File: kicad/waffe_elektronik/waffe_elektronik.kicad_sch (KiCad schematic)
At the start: 61 parts, among them J1 WS2812 HP-Streifen, J2 GX16-7pol, M1 Vibromotor Rueckstoß, M2 Vibromotor Treffer, Q1 AO3400A, Q2 AO3400A, Q3 AO3400A, SW1 Taster, SW2 Taster, U1 Boost_5V_MT3608, U10 TSOP34838, U11 TSOP34838, U2 AMS1117-3.3, U3 MCP73831, U4 ESP32S3_DevKitC, U5 74AHCT125, U6 MAX98357A, U7 TSOP34838, U8 TSOP34838, U9 TSOP34838

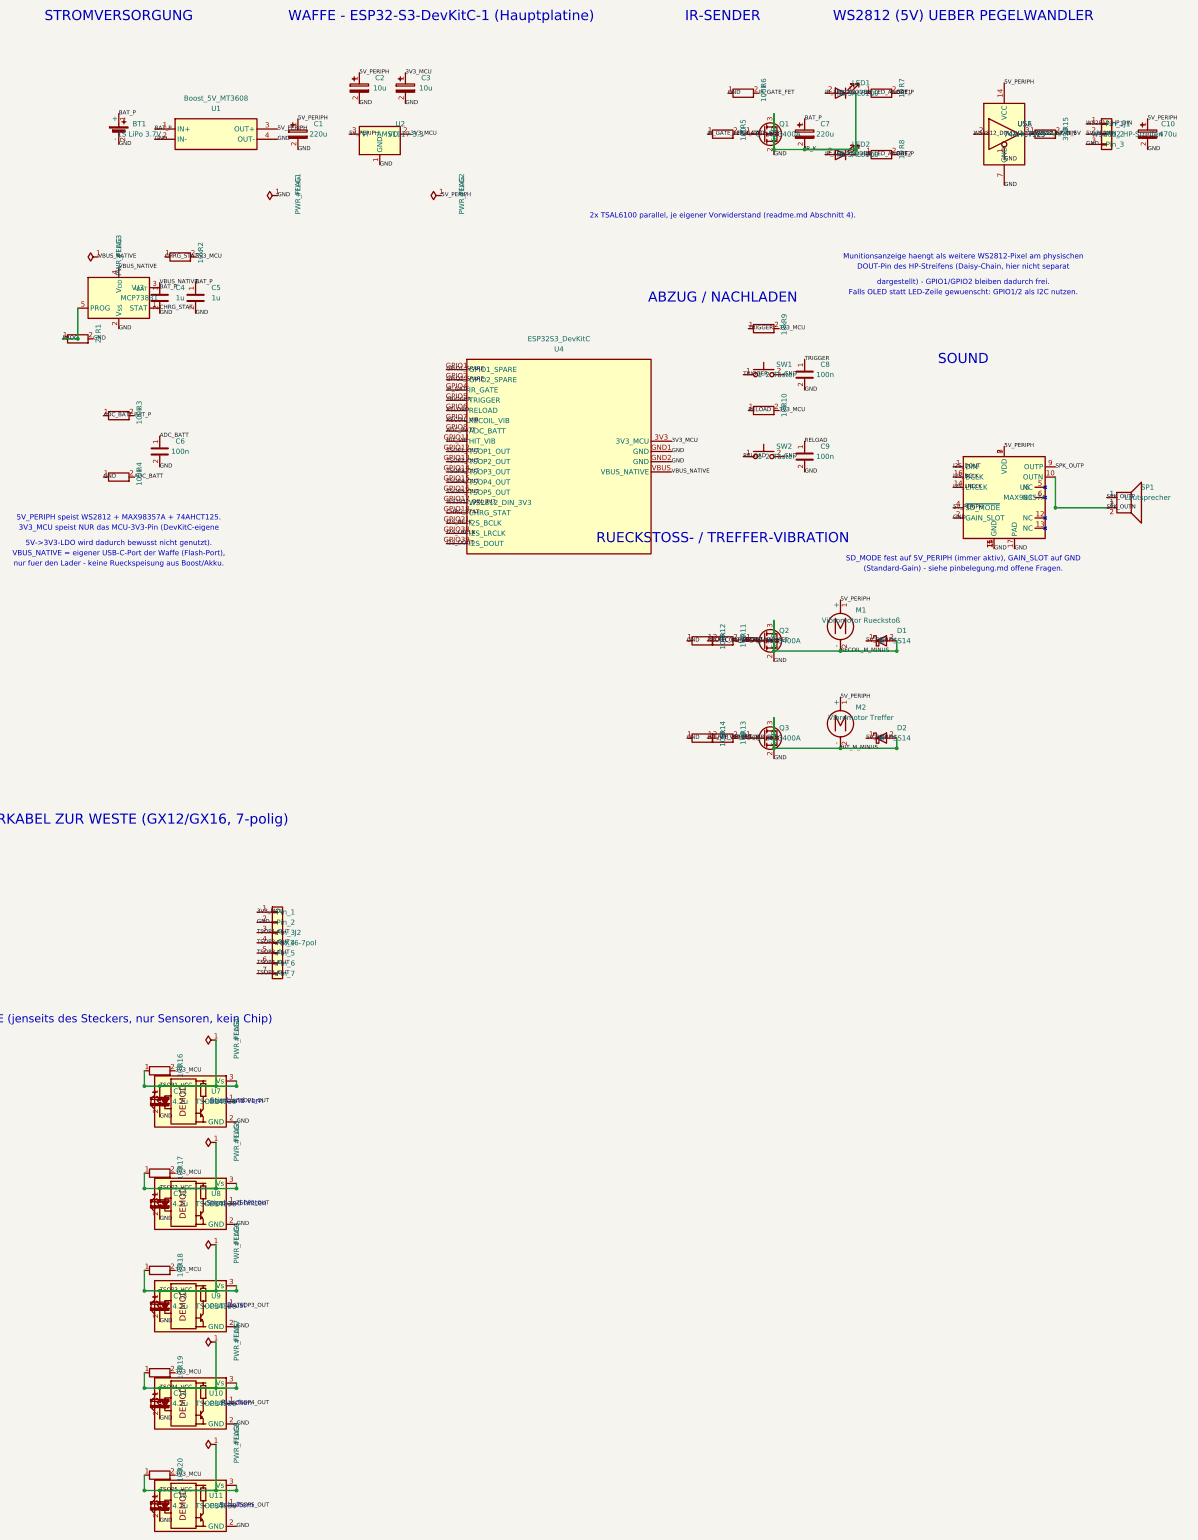
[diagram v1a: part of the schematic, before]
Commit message: Verdrahte alle Signalnetze echt (inkl. MCU-Läufe) statt nur lokaler Cluster
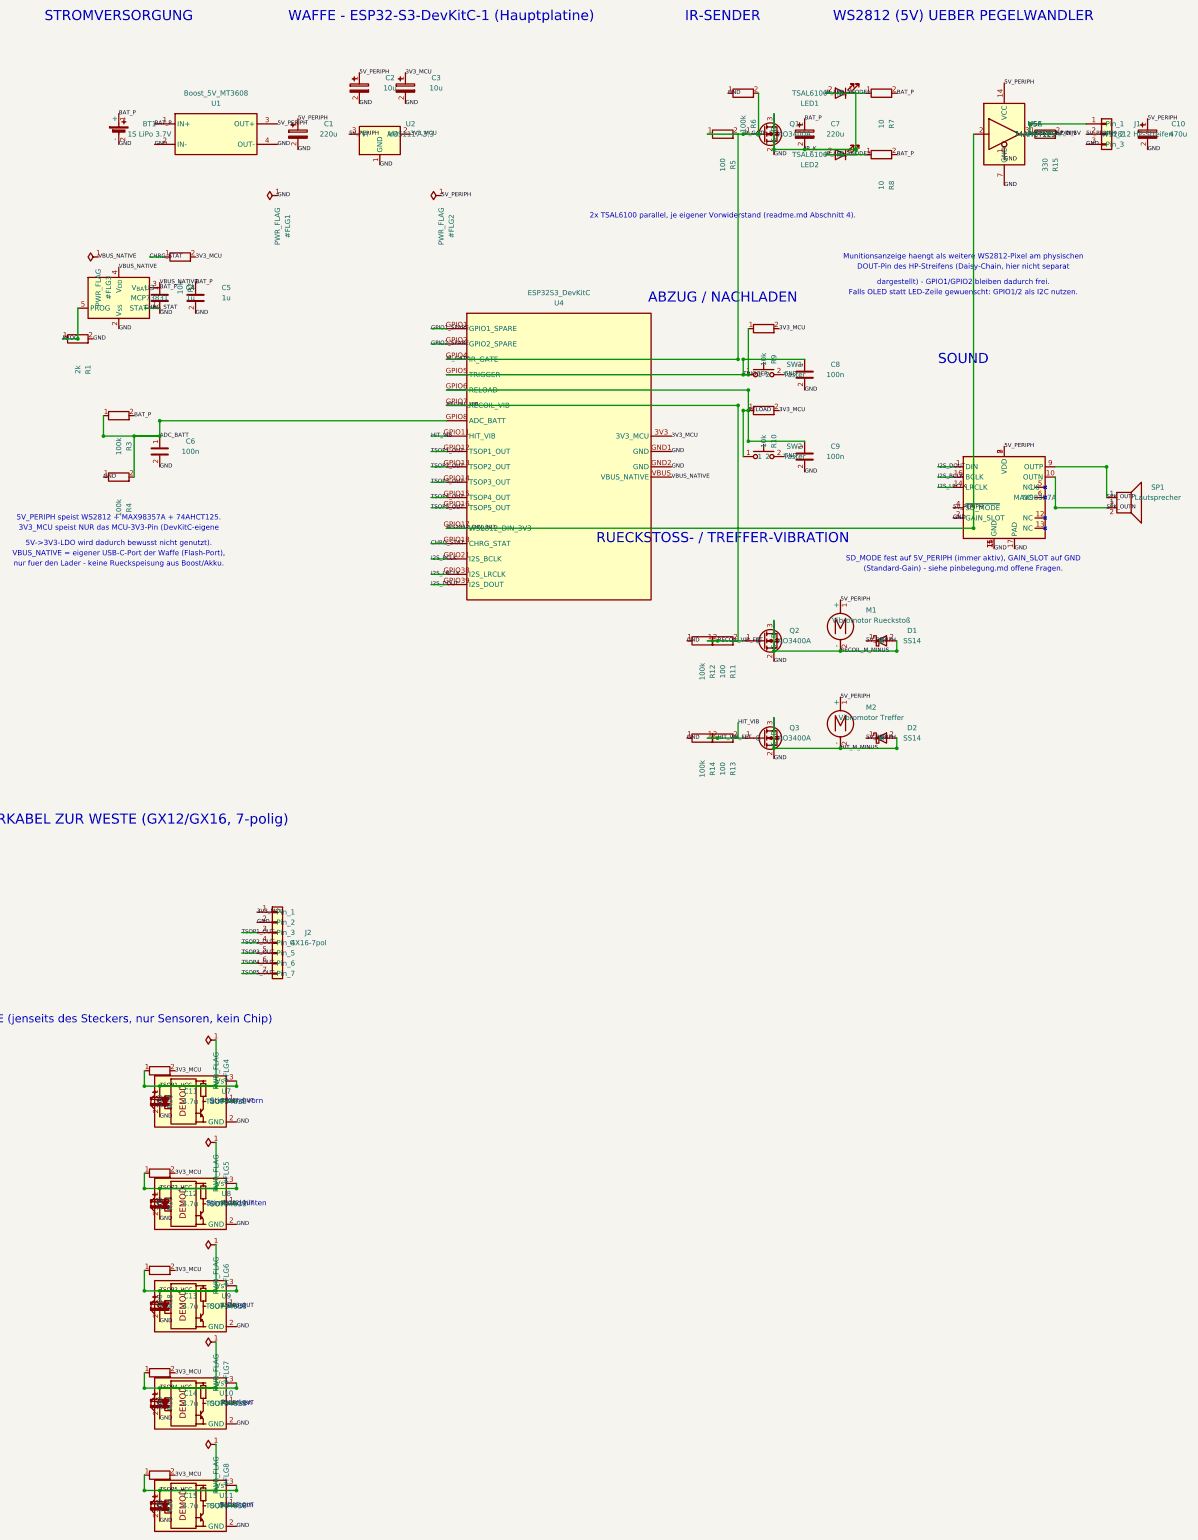
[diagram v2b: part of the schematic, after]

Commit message: Zeichne Schaltplan neu: Funktionsblöcke, saubere Verdrahtung, A3
Blöcke gerahmt, Versorgung oben/Masse unten, Signale zwischen Blöcken über
Labels an kurzen Stichleitungen. Unbenutzte 74AHCT125-Gatter auf GND,
GPIO1/2 als No-Connect. Vorschaubild in der README.
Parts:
- added unit 3 of U5
- added unit 2 of U5
- added unit 4 of U5
- BT1: value 1S LiPo 3.7V -> 1S LiPo 3,7 V
- J2: value GX16-7pol -> GX16 7-polig
- M1: value Vibromotor Rueckstoß -> Vibromotor Rückstoss
- U1: value Boost_5V_MT3608 -> MT3608 Boost 5 V
- U4: value ESP32S3_DevKitC -> ESP32-S3-DevKitC-1
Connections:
- net 3V3_MCU: now also R10.1, R16.1, R17.1, R18.1, R19.1, R2.1, R20.1, R9.1; no longer R10.2, R16.2, R17.2, R18.2, R19.2, R2.2, R20.2, R9.2
- net ADC_BATT: now also R3.2, R4.1; no longer R3.1, R4.2
- net BAT_P: now also R3.1, R7.1, R8.1; no longer R3.2, R7.2, R8.2
- net CHRG_STAT: now also R2.2; no longer R2.1
- net GND: now also R12.2, R14.2, R4.2, R6.2, U5.10, U5.12, U5.13, U5.4, U5.5, U5.9; no longer R12.1, R14.1, R4.1, R6.1
- net HIT_VIB: now also R13.1; no longer R13.2
- net IR_GATE: now also R5.1; no longer R5.2
- net RECOIL_VIB: now also R11.1; no longer R11.2
- net RELOAD: now also R10.2; no longer R10.1
- net TRIGGER: now also R9.2; no longer R9.1
- net GPIO1_SPARE: no longer names the net of U4.GPIO1
- net GPIO2_SPARE: no longer names the net of U4.GPIO2
- net HIT_M_MINUS: no longer names the net of D2.2 (A), M2.2 (-), Q3.3 (D)
- removed net HIT_VIB_FET: Q3.1 (G), R13.1, R14.2
- removed net IR_GATE_FET: Q1.1 (G), R5.1, R6.2
- net IR_K: no longer names the net of C7.2, LED1.1 (K), LED2.1 (K), Q1.3 (D)
- net IR_LED_ANODE1: no longer names the net of LED1.2 (A)
- net IR_LED_ANODE1: now also R7.2; no longer R7.1
- net IR_LED_ANODE2: no longer names the net of LED2.2 (A)
- net IR_LED_ANODE2: now also R8.2; no longer R8.1
- net PROG: no longer names the net of R1.1, U3.5 (PROG)
- net RECOIL_M_MINUS: no longer names the net of D1.2 (A), M1.2 (-), Q2.3 (D)
- removed net RECOIL_VIB_FET: Q2.1 (G), R11.1, R12.2
- net SPK_OUTN: no longer names the net of SP1.2, U6.10 (OUTN)
- net SPK_OUTP: no longer names the net of SP1.1, U6.9 (OUTP)
- net TSOP1_VCC: no longer names the net of C11.1, U7.3 (Vs)
- net TSOP1_VCC: now also R16.2; no longer R16.1
- net TSOP2_VCC: no longer names the net of C12.1, U8.3 (Vs)
- net TSOP2_VCC: now also R17.2; no longer R17.1
- net TSOP3_VCC: no longer names the net of C13.1, U9.3 (Vs)
- net TSOP3_VCC: now also R18.2; no longer R18.1
- net TSOP4_VCC: no longer names the net of C14.1, U10.3 (Vs)
- net TSOP4_VCC: now also R19.2; no longer R19.1
- net TSOP5_VCC: no longer names the net of C15.1, U11.3 (Vs)
- net TSOP5_VCC: now also R20.2; no longer R20.1
- net WS2812_DIN_5V: no longer names the net of U5.3
- net WS2812_DIN_5V: now also R15.1; no longer R15.2
- net WS2812_HP_DIN: no longer names the net of J1.1 (Pin_1)
- net WS2812_HP_DIN: now also R15.2; no longer R15.1
- new net: Q1.1 (G), R5.2, R6.1
- new net: Q3.1 (G), R13.2, R14.1
- new net: Q2.1 (G), R11.2, R12.1
- no-connect marks 0 -> 5
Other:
- note added: "Abzug / Nachladen"
- note added: "Akku-Messung"
- note added: "ESP32-S3 (Hauptplatine)"
- note added: "GPIO1/2 frei (Munitions-LED / I²C)"
- note added: "IR-Sender (2× TSAL6100 parallel)"
- note added: "Laden (USB-C Flash-Port)"
- note added: "Rücken"
- note added: "Rückstoss- / Treffer-Vibration"
- note added: "Sensorkabel zur Weste"
- note added: "Sound (I²S)"
- note added: "Stromversorgung"
- note added: "WS2812 (5 V) über Pegelwandler"
- note added: "Weste (nur Sensoren, jenseits des Steckers)"
- note added: "unbenutzte Gatter: Eingänge + /OE auf GND"
- note removed: "(Standard-Gain) - siehe pinbelegung.md offene Fragen."
- note removed: "2x TSAL6100 parallel, je eigener Vorwiderstand (readme.md Abschnitt 4)."
- note removed: "3V3_MCU speist NUR das MCU-3V3-Pin (DevKitC-eigene"
- note removed: "5V->3V3-LDO wird dadurch bewusst nicht genutzt)."
- note removed: "5V_PERIPH speist WS2812 + MAX98357A + 74AHCT125."
- note removed: "ABZUG / NACHLADEN"
- note removed: "DOUT-Pin des HP-Streifens (Daisy-Chain, hier nicht separat"
- note removed: "Falls OLED statt LED-Zeile gewuenscht: GPIO1/2 als I2C nutzen."
- note removed: "IR-SENDER"
- note removed: "Munitionsanzeige haengt als weitere WS2812-Pixel am physischen"
- note removed: "RUECKSTOSS- / TREFFER-VIBRATION"
- note removed: "Ruecken"
- note removed: "SD_MODE fest auf 5V_PERIPH (immer aktiv), GAIN_SLOT auf GND"
- note removed: "SENSORKABEL ZUR WESTE (GX12/GX16, 7-polig)"
- note removed: "SOUND"
- note removed: "STROMVERSORGUNG"
- note removed: "VBUS_NATIVE = eigener USB-C-Port der Waffe (Flash-Port),"
- note removed: "WAFFE - ESP32-S3-DevKitC-1 (Hauptplatine)"
- note removed: "WESTE (jenseits des Steckers, nur Sensoren, kein Chip)"
- note removed: "WS2812 (5V) UEBER PEGELWANDLER"
- note removed: "dargestellt) - GPIO1/GPIO2 bleiben dadurch frei."
- note removed: "nur fuer den Lader - keine Rueckspeisung aus Boost/Akku."
- company: (none) -> open-lasertag
- title: (none) -> Lasertag - Waffen-Elektronik

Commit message: ESP32-S3-WROOM-1 direkt auf der Platine, eigene USB-C-Buchse mit Auto-Flash
USB-C am nativen USB (IO19/IO20) mit CC-Widerständen und USBLC6-ESD-Schutz,
EN-RC-Glied, RESET- und BOOT-Taster. Flashen über USB-Serial-JTAG ohne
Wandlerchip. Doku und Stückliste angepasst.
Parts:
- removed U4: ESP32-S3-DevKitC-1, symbol Module:ESP32S3_DevKitC
- added C16: 1u, symbol Device:C
- added C17: 100n, symbol Device:C
- added C18: 10u, symbol Device:C
- added J3: USB-C (Flashen + Laden), symbol Connector:USB_C_Receptacle_USB2.0_16P
- added R21: 10k, symbol Device:R
- added R22, R23: 5.1k, symbol Device:R
- added SW3: RESET, symbol Switch:SW_Push
- added SW4: BOOT, symbol Switch:SW_Push
- added U12: USBLC6-2SC6, symbol Power_Protection:USBLC6-2SC6
- added U4: ESP32-S3-WROOM-1-N16R8, symbol RF_Module:ESP32-S3-WROOM-1
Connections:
- net 3V3_MCU: now also C17.1, C18.1, R21.1, U4.2 (3V3)
- net ADC_BATT: now also U4.12 (IO8)
- net CHRG_STAT: now also U4.11 (IO18)
- net GND: now also C16.2, C17.2, C18.2, J3.A1 (GND), J3.A12 (GND), J3.B1 (GND), J3.B12 (GND), J3.SH (SHIELD), R22.2, R23.2, SW3.1, SW4.1, U12.2 (GND), U4.1 (GND), U4.40 (GND), U4.41 (GND)
- net HIT_VIB: now also U4.19 (IO11)
- net I2S_BCLK: now also U4.23 (IO21)
- net I2S_DOUT: now also U4.32 (IO39)
- net I2S_LRCLK: now also U4.31 (IO38)
- net IR_GATE: now also U4.4 (IO4)
- net RECOIL_VIB: now also U4.7 (IO7)
- net RELOAD: now also U4.6 (IO6)
- net TRIGGER: now also U4.5 (IO5)
- net TSOP1_OUT: now also U4.20 (IO12)
- net TSOP2_OUT: now also U4.21 (IO13)
- net TSOP3_OUT: now also U4.22 (IO14)
- net TSOP4_OUT: now also U4.8 (IO15)
- net TSOP5_OUT: now also U4.9 (IO16)
- net VBUS_NATIVE: now also J3.A4 (VBUS), J3.A9 (VBUS), J3.B4 (VBUS), J3.B9 (VBUS), U12.5 (VBUS)
- net WS2812_DIN_3V3: now also U4.10 (IO17)
- new net: J3.A5 (CC1), R23.1
- new net: J3.A6 (D+), J3.B6 (D+), U12.3 (I/O2)
- new net: J3.A7 (D-), J3.B7 (D-), U12.1 (I/O1)
- new net: J3.B5 (CC2), R22.1
- new net: C16.1, R21.2, SW3.2, U4.3 (EN)
- new net: SW4.2, U4.27 (IO0)
- new net USB_D+: U12.4 (I/O2), U4.14 (USB_D+)
- new net USB_D-: U12.6 (I/O1), U4.13 (USB_D-)
- no-connect marks 5 -> 22
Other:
- note added: "ESP32-S3-WROOM-1"
- note added: "IO40 reserviert: TSOP 6 (Waffe vorne)"
- note added: "Laden (USB-C)"
- note added: "USB-C (nativer USB des ESP32-S3)"
- note added: "frei: IO1/IO2 (Munitions-LED / I²C), IO9/IO10, IO41/42, IO47/48"
- note removed: "ESP32-S3 (Hauptplatine)"
- note removed: "GPIO1/2 frei (Munitions-LED / I²C)"
- note removed: "Laden (USB-C Flash-Port)"

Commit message: Platine: 4 Lagen, nur SMD, von Hand geroutet; GPIOs layoutgetrieben neu zugeordnet
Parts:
- removed C1, C7: 220u, symbol Device:C_Polarized
- removed C10: 470u, symbol Device:C_Polarized
- removed C2: 10u, symbol Device:C_Polarized
- removed U1: MT3608 Boost 5 V, symbol Module:Boost_5V_MT3608
- added C1, C10, C7: 100u, Capacitor_SMD:C_1210_3225Metric, symbol Device:C
- added C19, C20: 22u, Capacitor_SMD:C_0805_2012Metric, symbol Device:C
- added C2, C22: 10u, Capacitor_SMD:C_0805_2012Metric, symbol Device:C
- added C21, C23: 100n, Capacitor_SMD:C_0603_1608Metric, symbol Device:C
- added D3: SS34, Diode_SMD:D_SMA, symbol Diode:SS34
- added L1: 22u, Inductor_SMD:L_Sunlord_MWSA0503S, symbol Device:L
- added R24: 75k, Resistor_SMD:R_0603_1608Metric, symbol Device:R
- added R25: 10k, Resistor_SMD:R_0603_1608Metric, symbol Device:R
- added U1: MT3608, Package_TO_SOT_SMD:SOT-23-6, symbol Regulator_Switching:MT3608
- BT1, SP1: footprint (none) -> Connector_JST:JST_PH_S2B-PH-SM4-TB_1x02-1MP_P2.00mm_Horizontal
- C16, C17, C4, C5, C6, C8, C9: footprint (none) -> Capacitor_SMD:C_0603_1608Metric
- C18: footprint (none) -> Capacitor_SMD:C_0805_2012Metric
- C3: footprint (none) -> Capacitor_Tantalum_SMD:CP_EIA-3528-21_Kemet-B
- D1, D2: footprint (none) -> Diode_SMD:D_SOD-123F
- J1: footprint (none) -> Connector_JST:JST_PH_S3B-PH-SM4-TB_1x03-1MP_P2.00mm_Horizontal
- J2: footprint (none) -> Connector_JST:JST_SH_SM07B-SRSS-TB_1x07-1MP_P1.00mm_Horizontal
- J3: footprint (none) -> Connector_USB:USB_C_Receptacle_GCT_USB4105-xx-A_16P_TopMnt_Horizontal
- LED1, LED2, M1, M2, SW1, SW2: footprint (none) -> Connector_JST:JST_SH_SM02B-SRSS-TB_1x02-1MP_P1.00mm_Horizontal
- Q1, Q2, Q3: footprint (none) -> Package_TO_SOT_SMD:SOT-23
- R1, R10, R11, R12, R13, R14, R15, R2, R21, R22, R23, R3, R4, R5, R6, R9: footprint (none) -> Resistor_SMD:R_0603_1608Metric
- R7, R8: footprint (none) -> Resistor_SMD:R_1206_3216Metric
- SW3, SW4: footprint (none) -> Button_Switch_SMD:SW_SPST_B3U-1000P
- U12: footprint (none) -> Package_TO_SOT_SMD:SOT-23-6
- U2: footprint (none) -> Package_TO_SOT_SMD:SOT-223-3_TabPin2
- U3: footprint (none) -> Package_TO_SOT_SMD:SOT-23-5
- U4: footprint (none) -> RF_Module:ESP32-S3-WROOM-1
- U5: footprint (none) -> Package_SO:TSSOP-14_4.4x5mm_P0.65mm
- U6: footprint (none) -> Package_DFN_QFN:TQFN-16-1EP_3x3mm_P0.5mm_EP1.23x1.23mm
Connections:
- net 5V_PERIPH: now also C1.1, C10.1, C2.1, C20.1, C21.1, C22.1, C23.1, D3.1 (K), R24.1
- net BAT_P: now also C19.1, C7.1, L1.1, U1.4 (EN), U1.5 (IN)
- net GND: now also C1.2, C10.2, C19.2, C2.2, C20.2, C21.2, C22.2, C23.2, R25.2, U1.2 (GND)
- net HIT_VIB: now also U4.24 (IO47); no longer U4.19 (IO11)
- net I2S_BCLK: now also U4.32 (IO39); no longer U4.23 (IO21)
- net I2S_DOUT: now also U4.31 (IO38); no longer U4.32 (IO39)
- net I2S_LRCLK: now also U4.33 (IO40); no longer U4.31 (IO38)
- net IR_GATE: now also U4.6 (IO6); no longer U4.4 (IO4)
- net RECOIL_VIB: now also U4.25 (IO48); no longer U4.7 (IO7)
- net RELOAD: now also U4.5 (IO5); no longer U4.6 (IO6)
- net TRIGGER: now also U4.4 (IO4); no longer U4.5 (IO5)
- net TSOP1_OUT: now also U4.18 (IO10); no longer U4.20 (IO12)
- net TSOP2_OUT: now also U4.19 (IO11); no longer U4.21 (IO13)
- net TSOP3_OUT: now also U4.20 (IO12); no longer U4.22 (IO14)
- net TSOP4_OUT: now also U4.21 (IO13); no longer U4.8 (IO15)
- net TSOP5_OUT: now also U4.22 (IO14); no longer U4.9 (IO16)
- net at LED1.1 (K), LED2.1 (K), Q1.3 (D): now also C7.2
- new net: D3.2 (A), L1.2, U1.1 (SW)
- new net: R24.2, R25.1, U1.3 (FB)
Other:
- note added: "IO21 reserviert: TSOP 6 (Waffe vorne)"
- note added: "frei: IO1/IO2 (Munitions-LED / I²C), IO7, IO9, IO15/16, IO41/42"
- note removed: "IO40 reserviert: TSOP 6 (Waffe vorne)"
- note removed: "frei: IO1/IO2 (Munitions-LED / I²C), IO9/IO10, IO41/42, IO47/48"

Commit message: JLCPCB-Bestellpaket: LCSC-Teile im Schaltplan, Gerber/BOM/CPL, Skill jlcpcb-order
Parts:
- BT1, SP1: LCSC (none) -> C225233
- C1, C10: LCSC (none) -> C723734
- C16, C4, C5: LCSC (none) -> C15849
- C17, C21, C23, C6, C8, C9: LCSC (none) -> C14663
- C18, C2, C22: LCSC (none) -> C15850
- C19, C20: LCSC (none) -> C45783
- C3: LCSC (none) -> C7193
- C7: LCSC (none) -> C49066
- D1, D2: LCSC (none) -> C2909920
- D3: LCSC (none) -> C8678
- J1: LCSC (none) -> C265101
- J2: LCSC (none) -> C160406
- J3: LCSC (none) -> C5184243
- L1: value 22u -> 10u; LCSC (none) -> C408412
- LED1, LED2, M1, M2, SW1, SW2: LCSC (none) -> C160402
- Q1, Q2, Q3: LCSC (none) -> C20917
- R1: LCSC (none) -> C22975
- R10, R2, R21, R25, R9: LCSC (none) -> C25804
- R11, R13, R5: LCSC (none) -> C22775
- R12, R14, R3, R4, R6: LCSC (none) -> C25803
- R15: LCSC (none) -> C23138
- R22, R23: LCSC (none) -> C23186
- R24: LCSC (none) -> C23242
- R7, R8: LCSC (none) -> C17903
- SW3, SW4: LCSC (none) -> C231329
- U1: LCSC (none) -> C84817
- U12: LCSC (none) -> C7519
- U2: LCSC (none) -> C6186
- U3: LCSC (none) -> C424093
- U4: LCSC (none) -> C2913202
- U5: value 74AHCT125 -> 74HCT125; LCSC (none) -> C131316
- U6: LCSC (none) -> C910544
